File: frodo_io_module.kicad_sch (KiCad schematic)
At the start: 33 parts, among them J1 Conn_01x04_Pin, J1 Molex MicroFit 2x3, J2 Molex MicroFit 2x3, J4 Conn_01x04_Pin, U1 AZ1117H-ADJ, U1 STM32F072RBT6, U3 AZ1117-3.3, U5 AZ1117-5.0, Y1 8MHz

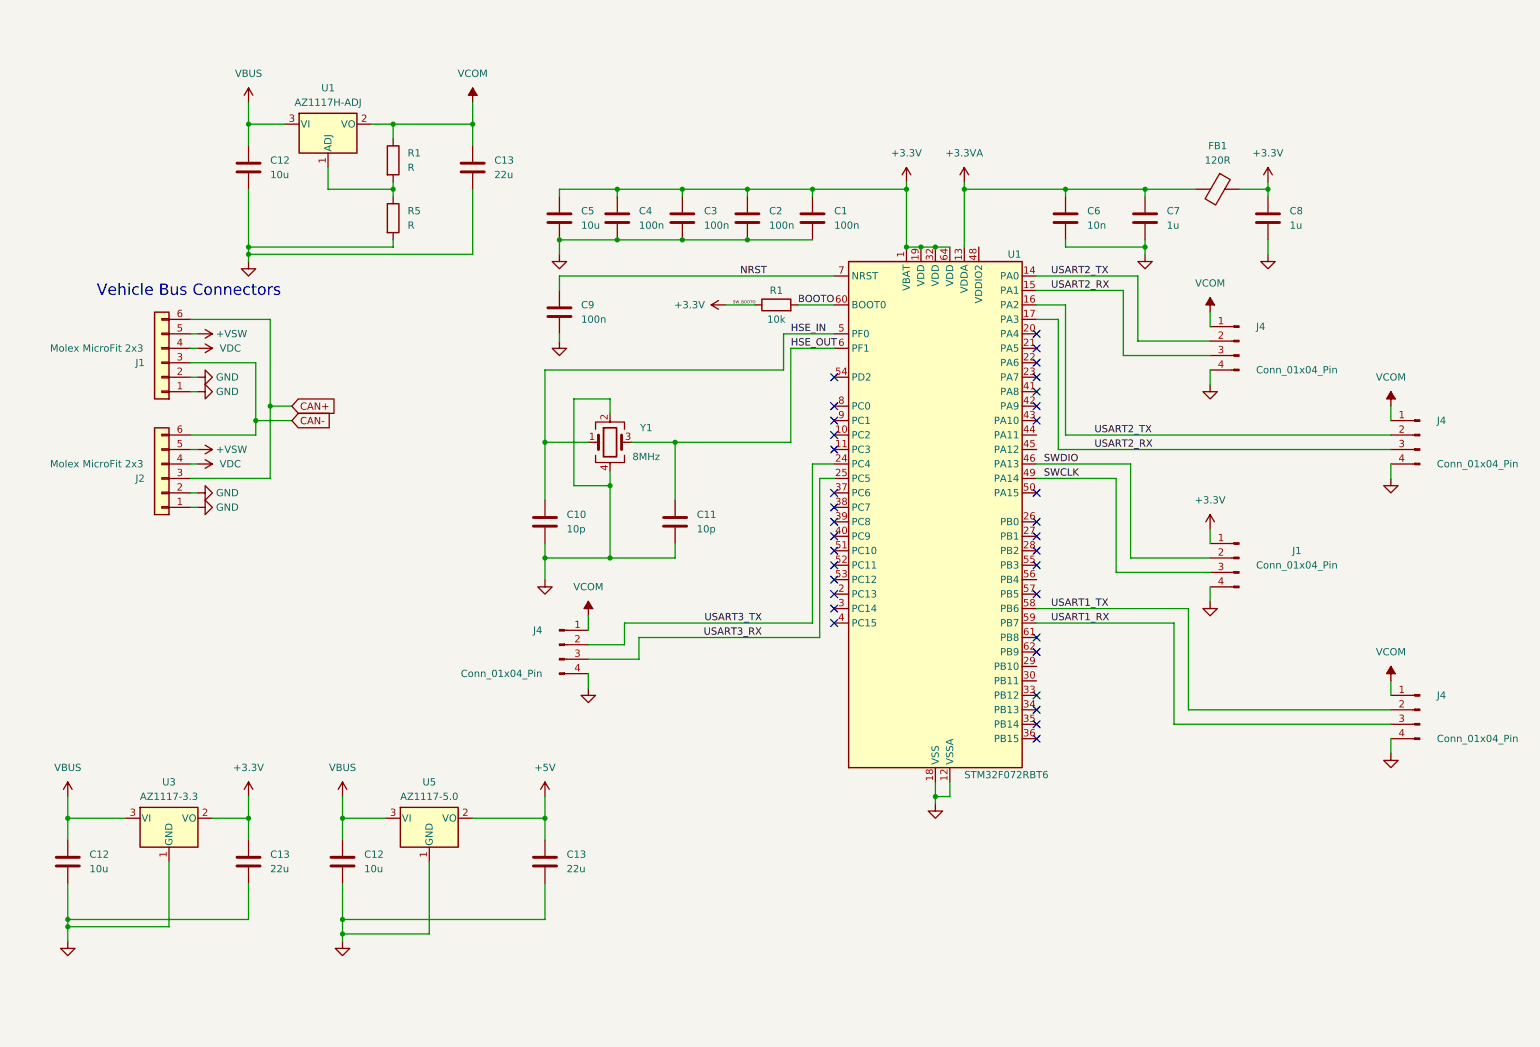
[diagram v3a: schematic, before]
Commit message: dip switch addition
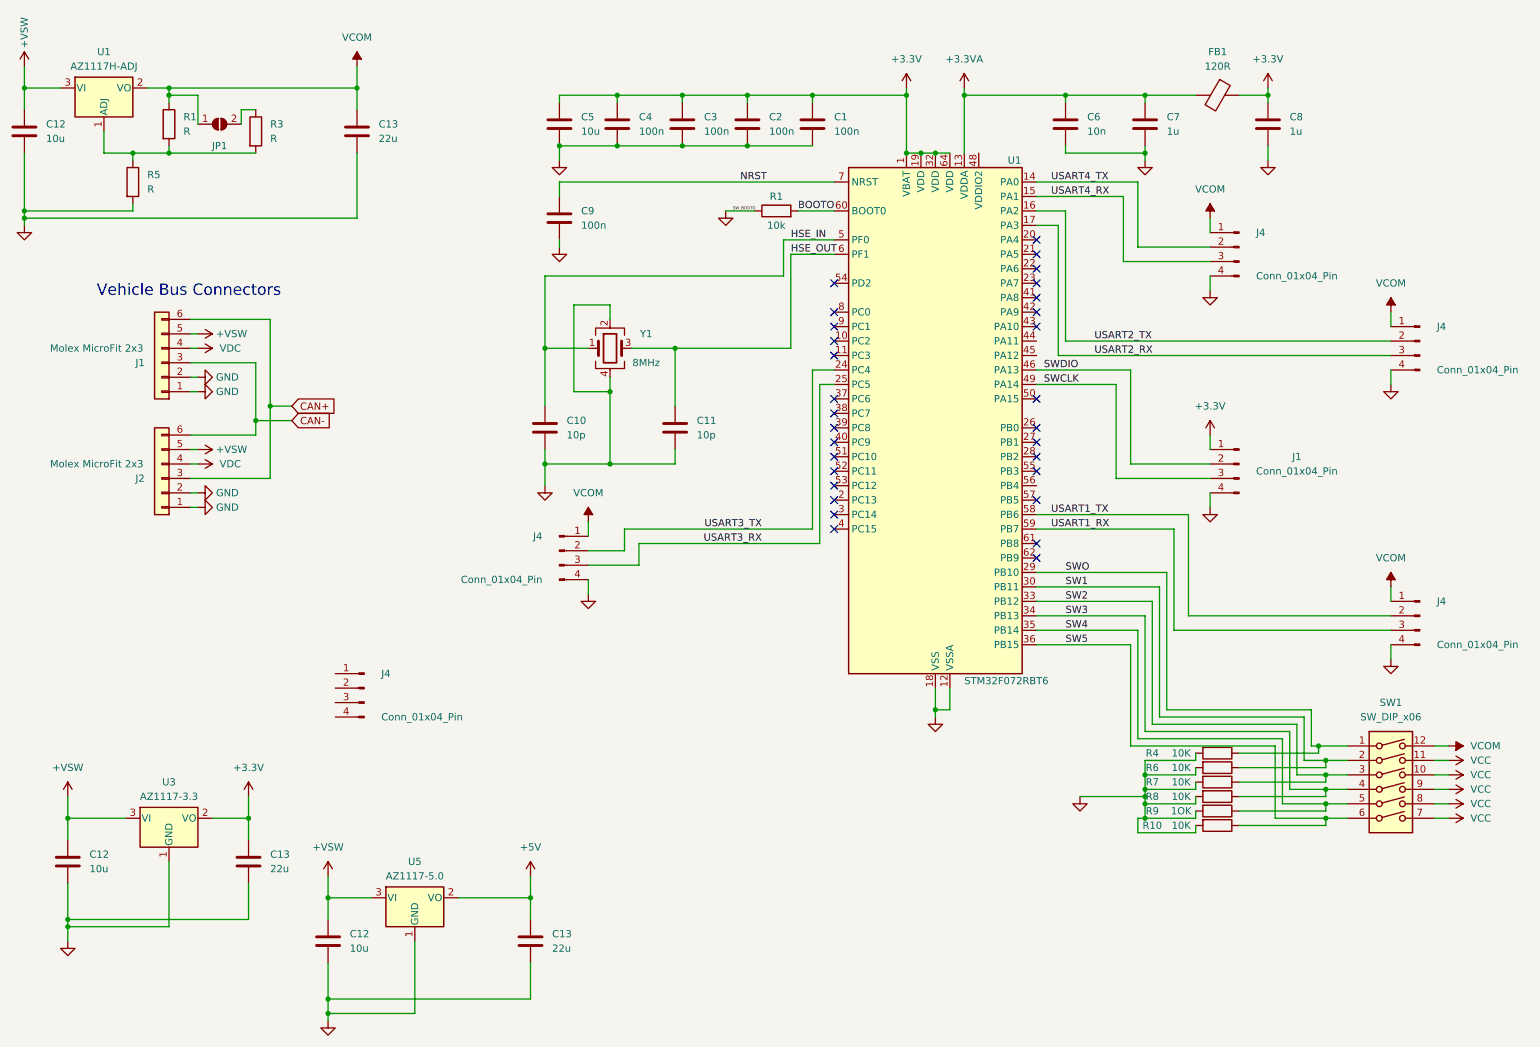
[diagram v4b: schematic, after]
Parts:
- added J4: Conn_01x04_Pin, symbol Connector:Conn_01x04_Pin
- added JP1: SolderJumper_2_Open, symbol Jumper:SolderJumper_2_Open
- added R10, R4, R6, R7, R8: 10K, symbol Device:R
- added R3: R, symbol Device:R
- added R9: 1OK, symbol Device:R
- added SW1: SW_DIP_x06, symbol Switch:SW_DIP_x06
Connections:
- net VBUS is gone; now on net +VSW: C12.1, C12.1, C12.1, U1.3 (VI), U3.3 (VI), U5.3 (VI)
- net +3.3V: no longer R1.1
- net GND: now also R1.1, R10.2, R4.2, R6.2, R7.2, R8.2, R9.2
- net USART2_RX: no longer J4.3 (Pin_3), U1.15 (PA1)
- net USART2_TX: no longer J4.2 (Pin_2), U1.14 (PA0)
- net VCOM: now also JP1.1 (A), SW1.12
- net at R1.2, R5.1, U1.1 (ADJ): now also R3.2
- net SWO: now reaches U1.29 (PB10)
- net SWO: now also R4.1, SW1.1
- net SW1: now reaches U1.30 (PB11)
- net SW1: now also R6.1, SW1.2
- net SW2: now reaches U1.33 (PB12)
- net SW2: now also R7.1, SW1.3
- net SW3: now reaches U1.34 (PB13)
- net SW3: now also R8.1, SW1.4
- net SW4: now reaches U1.35 (PB14)
- net SW4: now also R9.1, SW1.5
- net SW5: now reaches U1.36 (PB15)
- net SW5: now also R10.1, SW1.6
- new net: JP1.2 (B), R3.1
- new net USART4_RX: J4.3 (Pin_3), U1.15 (PA1)
- new net USART4_TX: J4.2 (Pin_2), U1.14 (PA0)
- new net VCC: SW1.10, SW1.11, SW1.7, SW1.8, SW1.9
- no-connect marks 34 -> 30
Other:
- moved on the sheet: C1, C10, C11, C12, C13, C2, C3, C4, C5, C6, C7, C8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

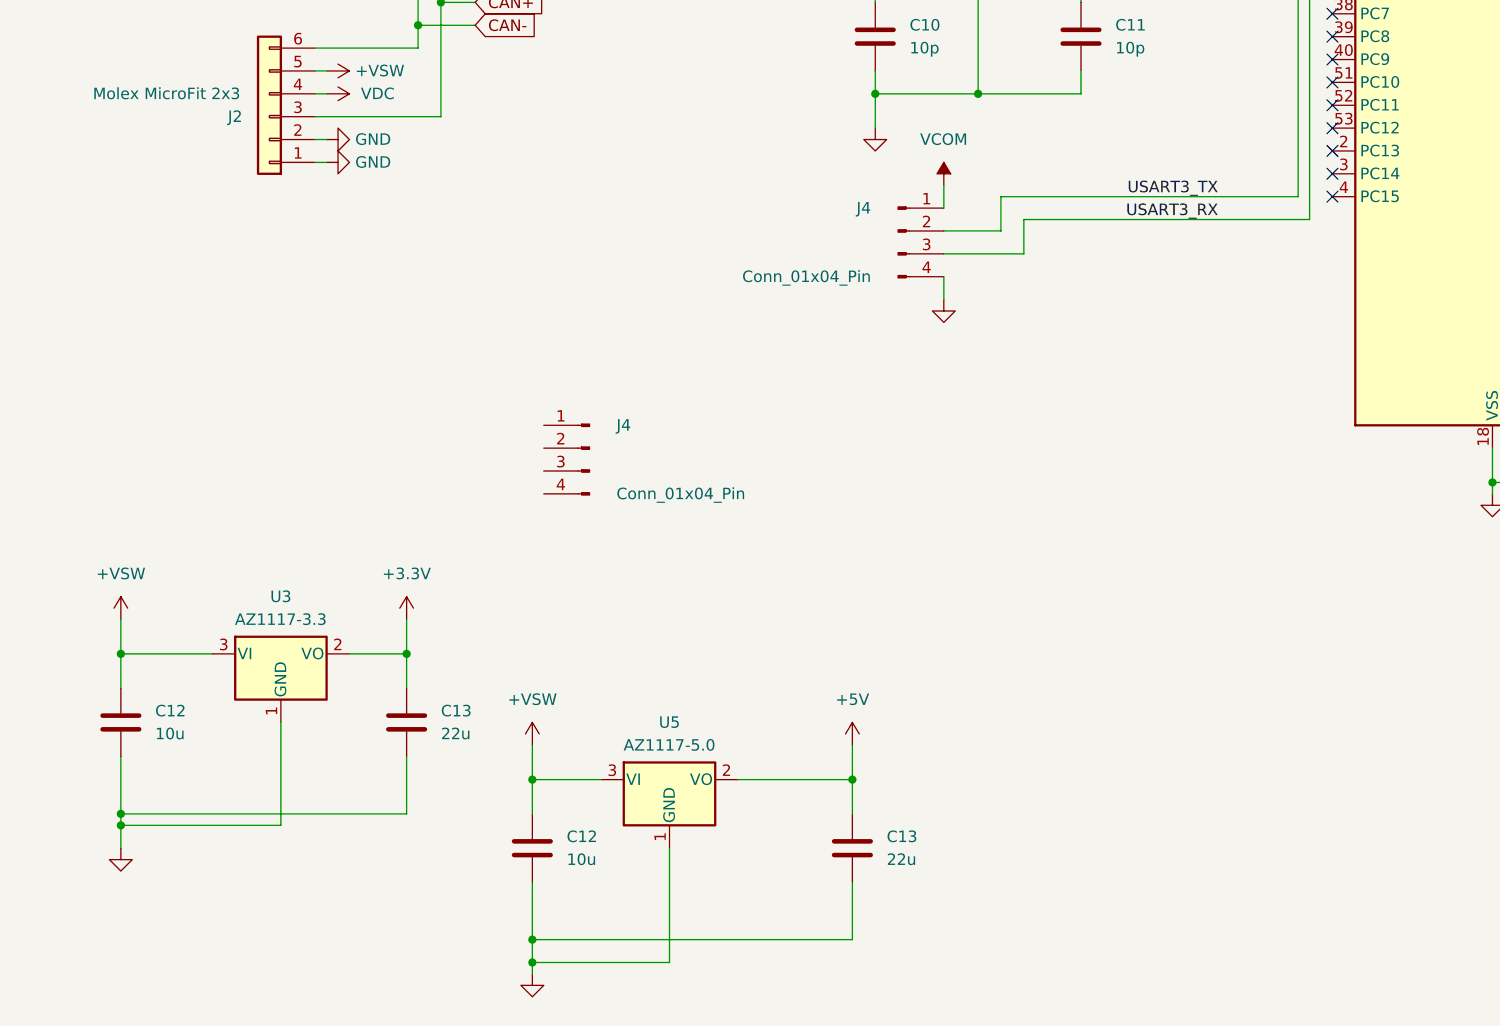
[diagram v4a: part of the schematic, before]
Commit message: mosfet addition
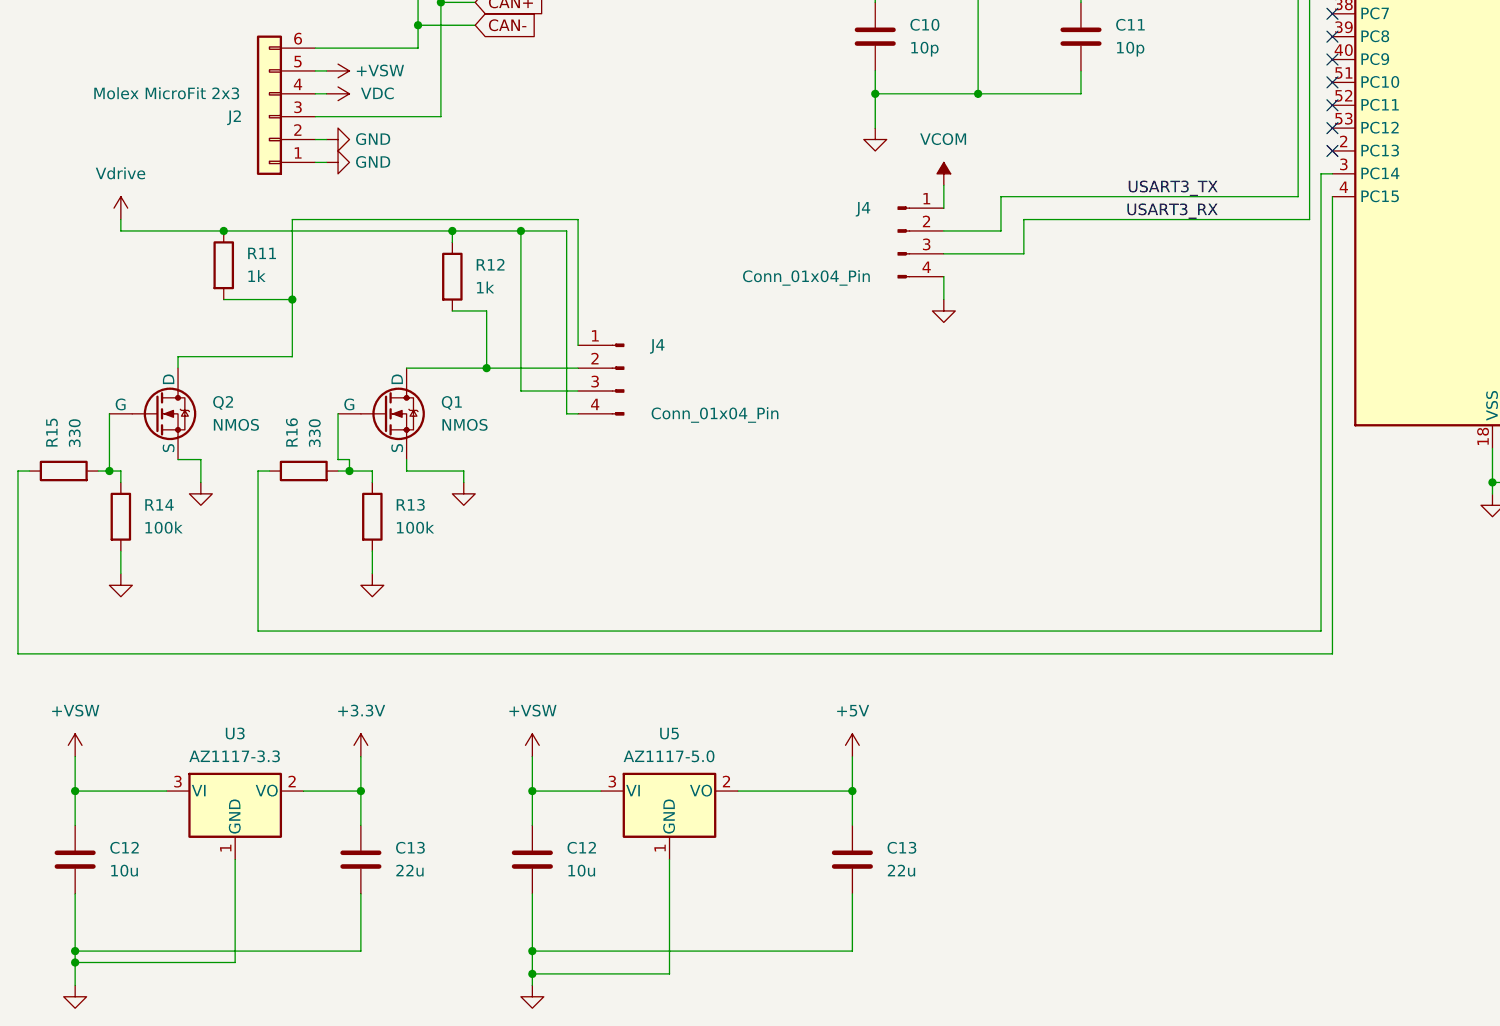
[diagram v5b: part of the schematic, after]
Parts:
- added Q1, Q2: NMOS, symbol Simulation_SPICE:NMOS
- added R11, R12: 1k, symbol Device:R
- added R13, R14: 100k, symbol Device:R
- added R15, R16: 330, symbol Device:R
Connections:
- net GND: now also Q1.3 (S), Q2.3 (S), R13.2, R14.2
- net at U1.3 (PC14): now also R16.1
- net at U1.4 (PC15): now also R15.1
- net at J4.1 (Pin_1): now also Q2.1 (D), R11.2
- net at J4.2 (Pin_2): now also Q1.1 (D), R12.2
- net Vdrive: now reaches J4.3 (Pin_3)
- net Vdrive: now also J4.4 (Pin_4), R11.1, R12.1
- new net: Q2.2 (G), R14.1, R15.2
- new net: Q1.2 (G), R13.1, R16.2
- no-connect marks 30 -> 28
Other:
- moved on the sheet: C12, C13, J4, U3, U5

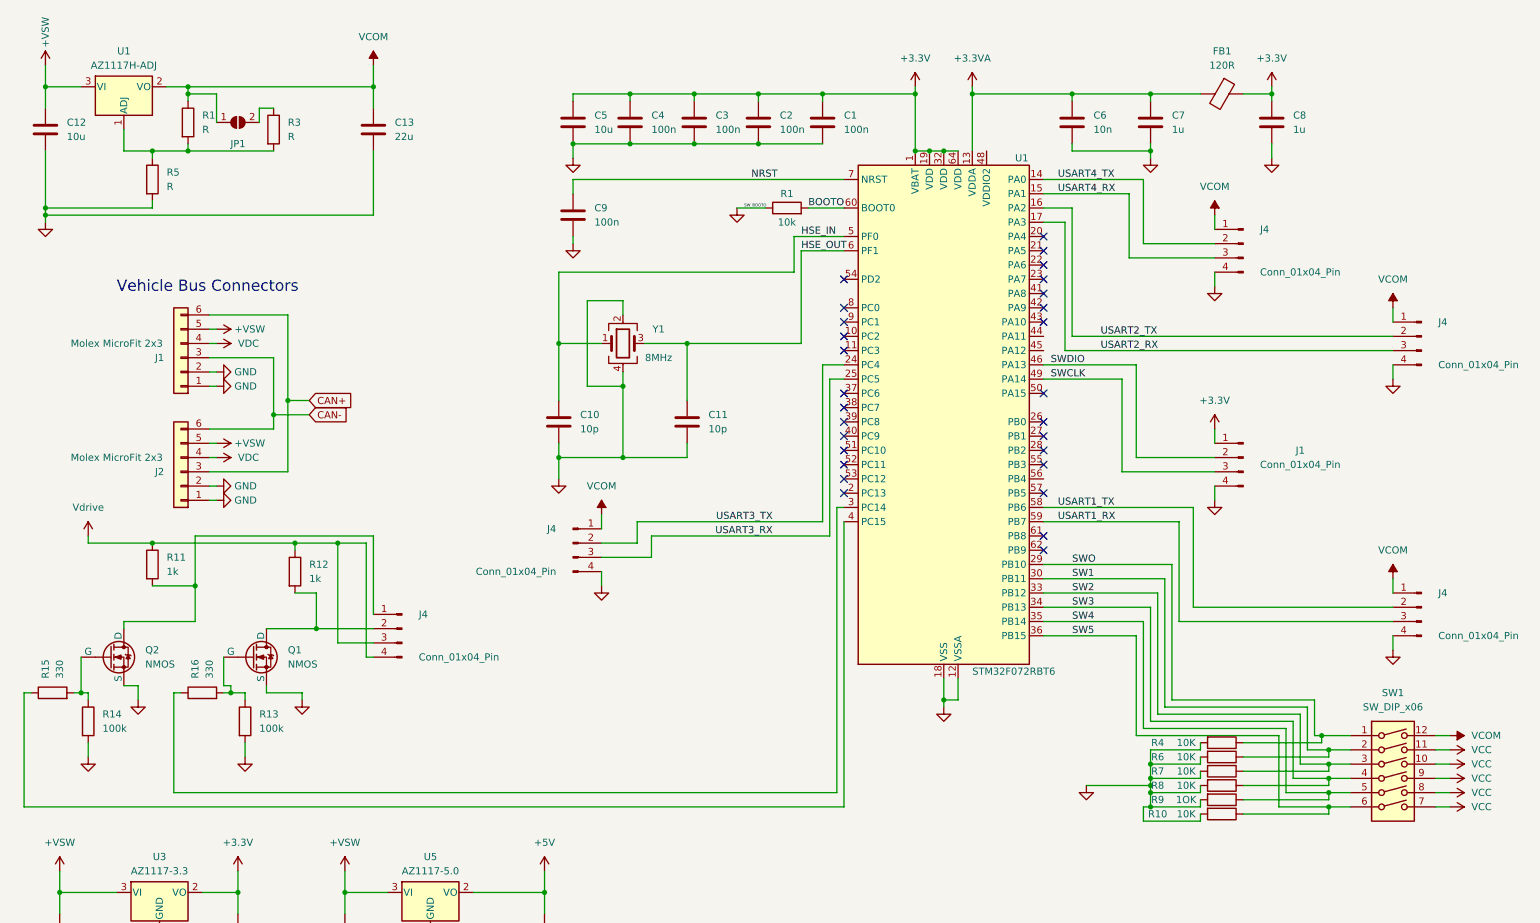
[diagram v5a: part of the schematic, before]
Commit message: label addition and switch changes
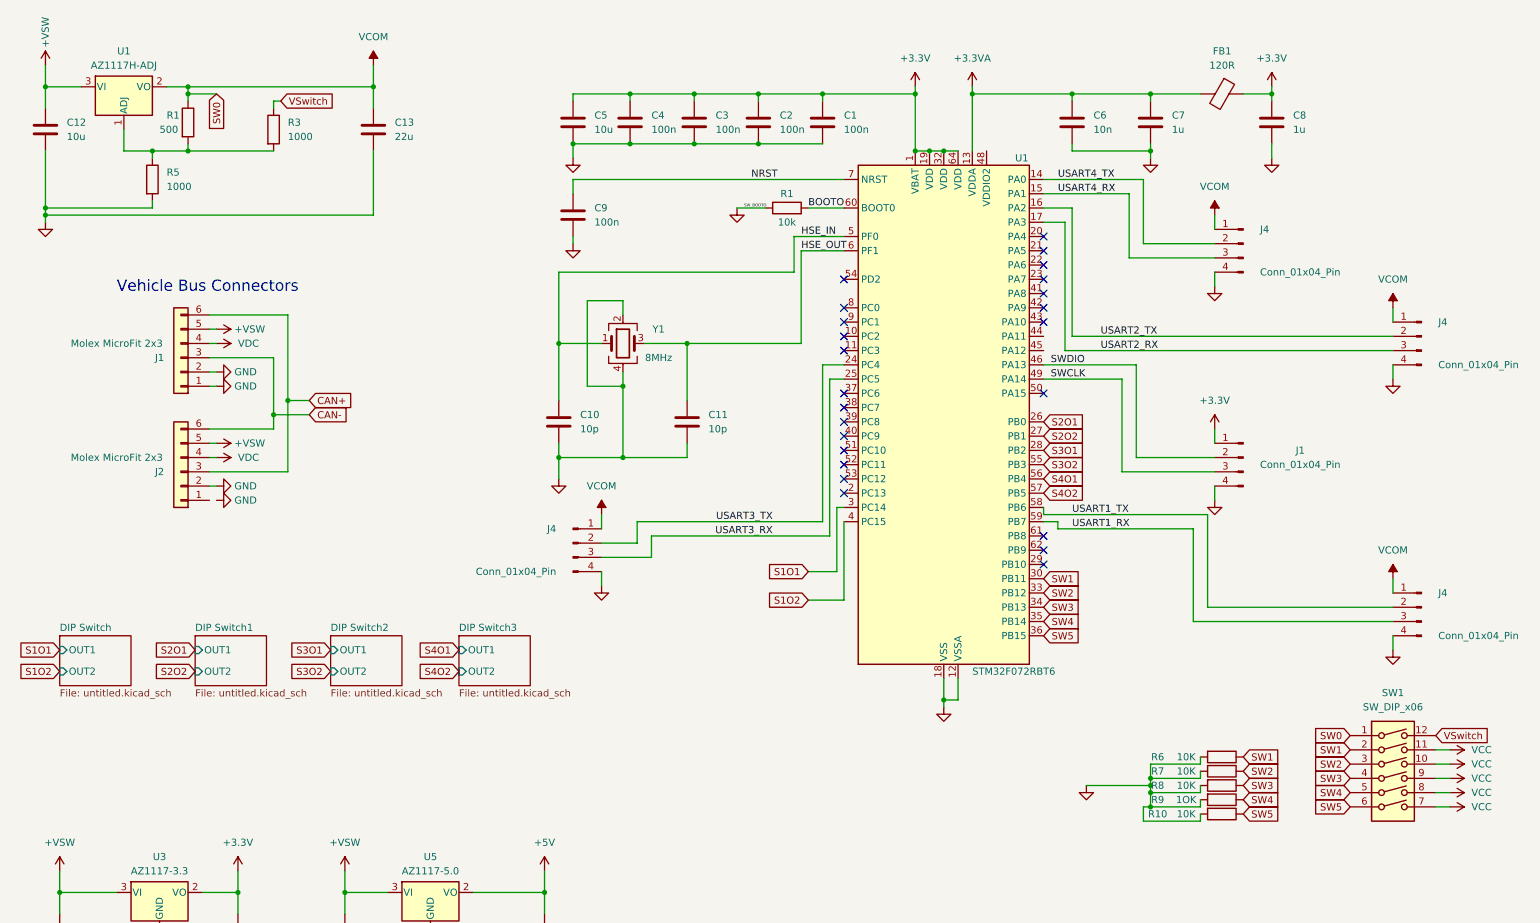
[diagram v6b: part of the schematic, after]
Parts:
- removed J4: Conn_01x04_Pin, symbol Connector:Conn_01x04_Pin
- removed JP1: SolderJumper_2_Open, symbol Jumper:SolderJumper_2_Open
- removed Q1, Q2: NMOS, symbol Simulation_SPICE:NMOS
- removed R11, R12: 1k, symbol Device:R
- removed R13, R14: 100k, symbol Device:R
- removed R15, R16: 330, symbol Device:R
- removed R4: 10K, symbol Device:R
- R1: value R -> 500
- R3, R5: value R -> 1000
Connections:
- net GND: no longer J2.1 (Pin_1)
- net VCOM: now also SW1.1; no longer SW1.12
- net S1O2: now reaches U1.4 (PC15)
- net VSwitch: now reaches R3.1
- net VSwitch: now also SW1.12
- net S1O1: now reaches U1.3 (PC14)
- net S2O1: now reaches U1.26 (PB0)
- net S2O2: now reaches U1.27 (PB1)
- net S3O1: now reaches U1.28 (PB2)
- net S3O2: now reaches U1.55 (PB3)
- net S4O1: now reaches U1.56 (PB4)
- net S4O2: now reaches U1.57 (PB5)
- net SWO: no longer names the net of U1.29 (PB10)
- net SWO: no longer SW1.1
- no-connect marks 28 -> 24
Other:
- added sheet DIP Switch (untitled.kicad_sch)
- added sheet DIP Switch1 (untitled.kicad_sch)
- added sheet DIP Switch2 (untitled.kicad_sch)
- added sheet DIP Switch3 (untitled.kicad_sch)
